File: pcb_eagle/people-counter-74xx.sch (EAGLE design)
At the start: 13 parts, among them IC1 74LS90N, IC2 74LS47N

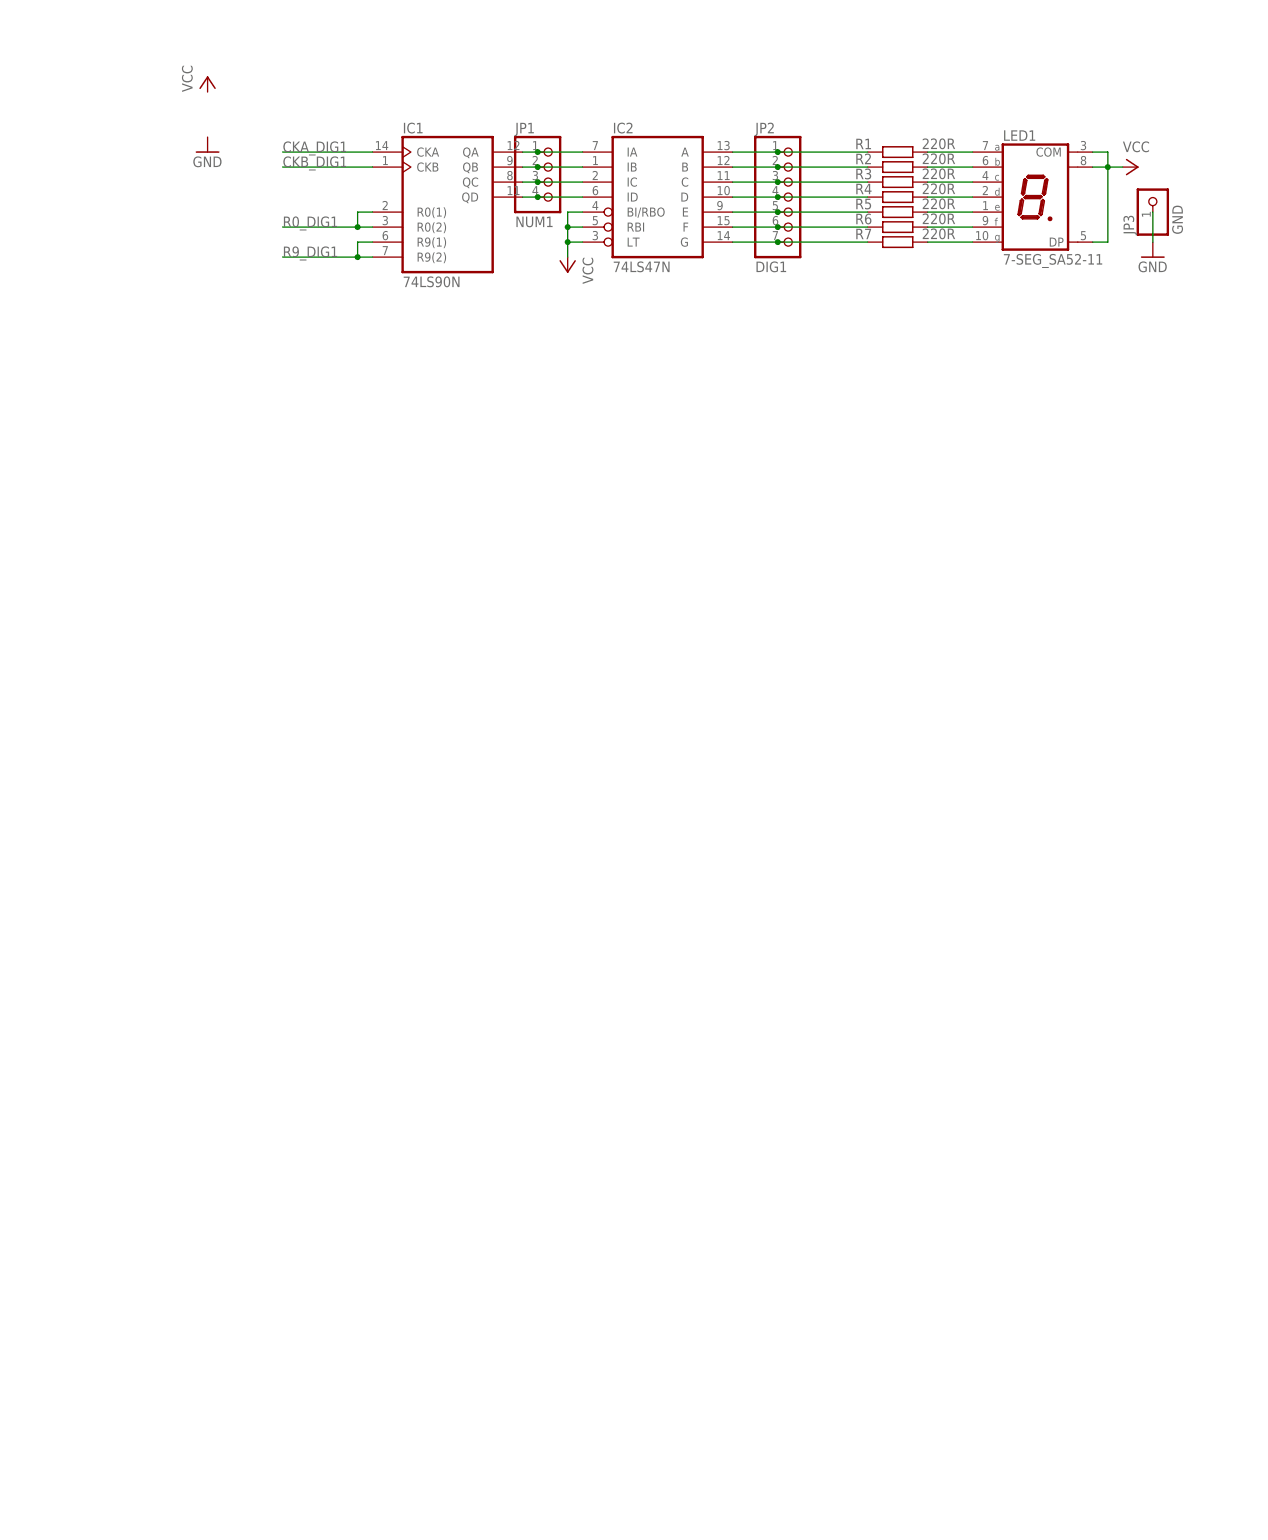
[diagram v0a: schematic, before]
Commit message: PCB_EAGLE: finish layout of 4 design module (LED segment counter}
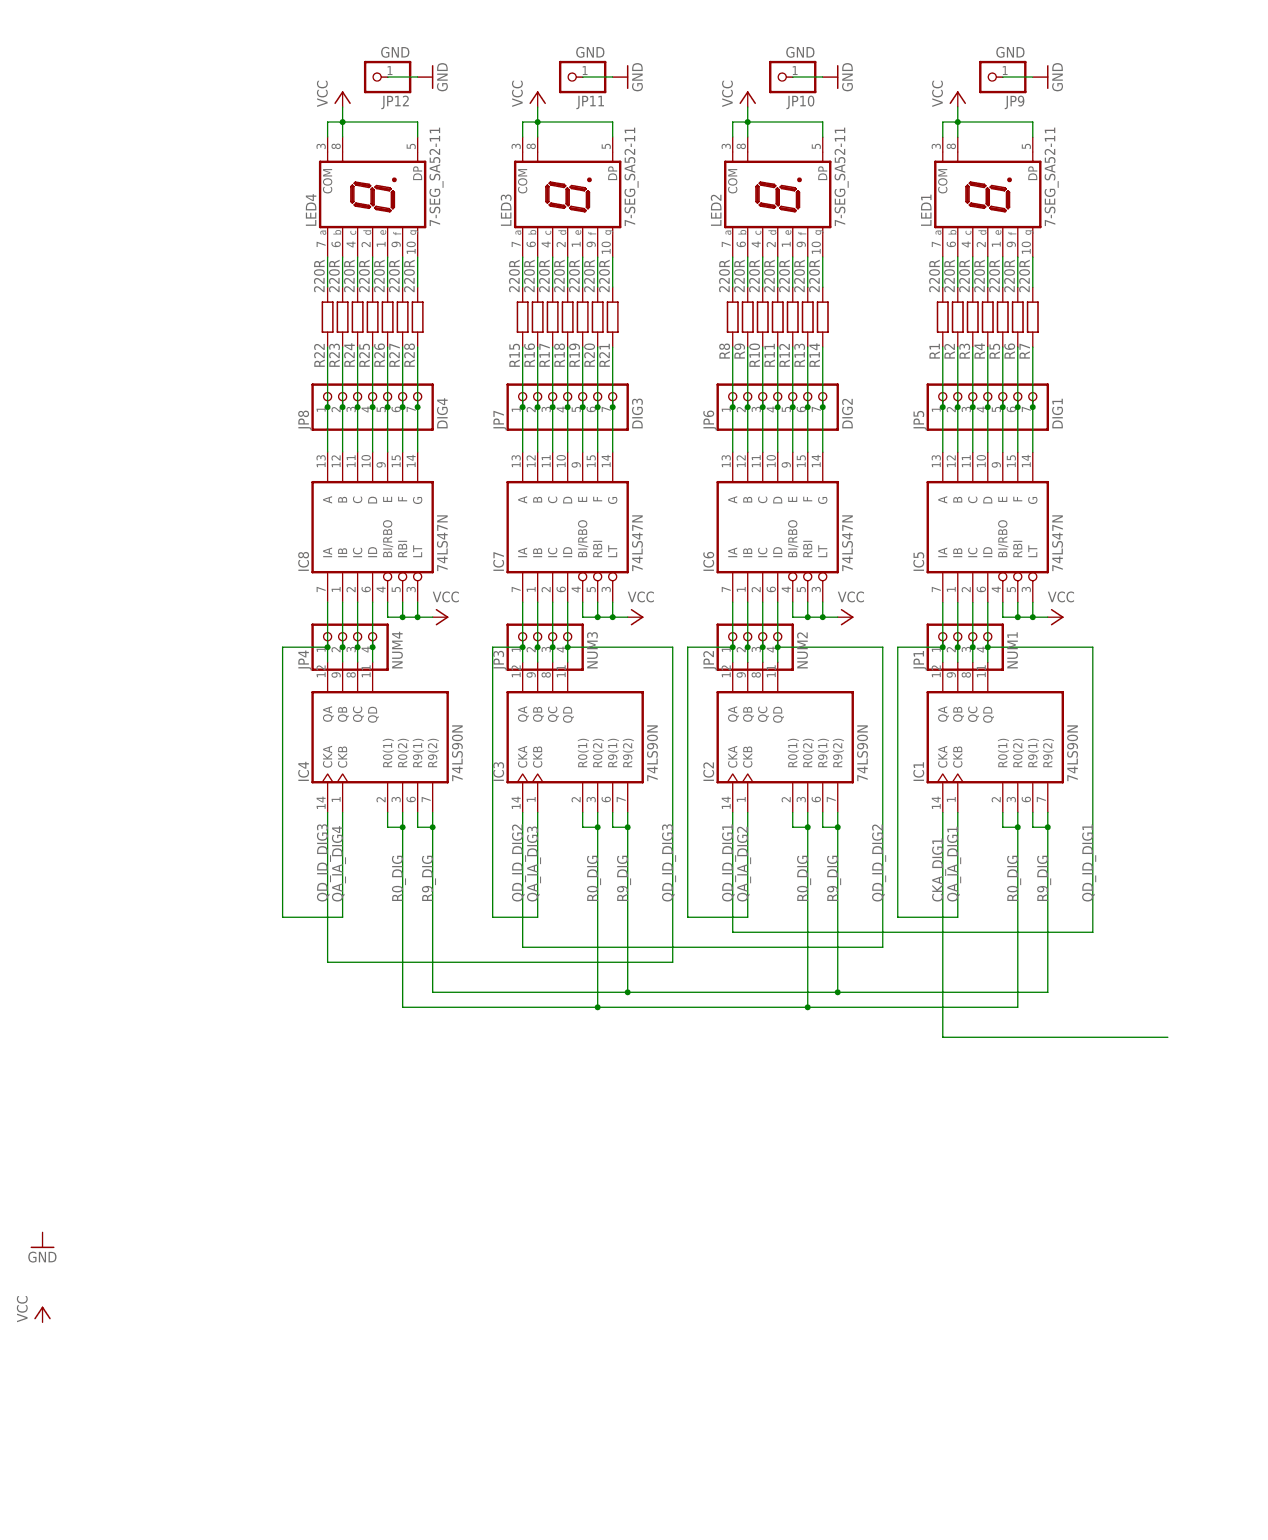
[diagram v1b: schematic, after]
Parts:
- added IC3, IC4: 74LS90N, 74xx-eu:74LS90N
- added IC5, IC6, IC7, IC8: 74LS47N, 74xx-eu:74LS47N
- added JP10, JP11, JP12, JP9: GND, pinhead:PINHD-1X1
- added JP4: NUM4, pinhead:PINHD-1X4
- added JP5: DIG1, pinhead:PINHD-1X7
- added JP6: DIG2, pinhead:PINHD-1X7
- added JP7: DIG3, pinhead:PINHD-1X7
- added JP8: DIG4, pinhead:PINHD-1X7
- added LED2, LED3, LED4: 7-SEG_SA52-11, display-kingbright:7-SEG_SA52-11
- added R10, R11, R12, R13, R14, R15, R16, R17, R18, R19, R20, R21, R22, R23, R24, R25, R26, R27, R28, R8, R9: 220R, rcl:R-EU_R0603
- IC2: value 74LS47N -> 74LS90N; device 74xx-eu:74LS47N -> 74xx-eu:74LS90N
- JP2: value DIG1 -> NUM2; device pinhead:PINHD-1X7 -> pinhead:PINHD-1X4
- JP3: value GND -> NUM3; device pinhead:PINHD-1X1 -> pinhead:PINHD-1X4
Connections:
- removed net CKB_DIG1: IC1A.CKB
- removed net R0_DIG1: IC1A.R0(1), IC1A.R0(2)
- removed net R9_DIG1: IC1A.R9(1), IC1A.R9(2)
- new net A_DIG2: IC6G$1.A, JP6.1, R8.1
- new net A_DIG3: IC7G$1.A, JP7.1, R15.1
- new net A_DIG4: IC8G$1.A, JP8.1, R22.1
- new net A_DIG_2: LED2.A, R8.2
- new net A_DIG_3: LED3.A, R15.2
- new net A_DIG_4: LED4.A, R22.2
- new net B_DIG2: IC6G$1.B, JP6.2, R9.1
- new net B_DIG3: IC7G$1.B, JP7.2, R16.1
- new net B_DIG4: IC8G$1.B, JP8.2, R23.1
- new net B_DIG_2: LED2.B, R9.2
- new net B_DIG_3: LED3.B, R16.2
- new net B_DIG_4: LED4.B, R23.2
- new net C_DIG2: IC6G$1.C, JP6.3, R10.1
- new net C_DIG3: IC7G$1.C, JP7.3, R17.1
- new net C_DIG4: IC8G$1.C, JP8.3, R24.1
- new net C_DIG_2: LED2.C, R10.2
- new net C_DIG_3: LED3.C, R17.2
- new net C_DIG_4: LED4.C, R24.2
- new net D_DIG2: IC6G$1.D, JP6.4, R11.1
- new net D_DIG3: IC7G$1.D, JP7.4, R18.1
- new net D_DIG4: IC8G$1.D, JP8.4, R25.1
- new net D_DIG_2: LED2.D, R11.2
- new net D_DIG_3: LED3.D, R18.2
- new net D_DIG_4: LED4.D, R25.2
- new net E_DIG2: IC6G$1.E, JP6.5, R12.1
- new net E_DIG3: IC7G$1.E, JP7.5, R19.1
- new net E_DIG4: IC8G$1.E, JP8.5, R26.1
- new net E_DIG_2: LED2.E, R12.2
- new net E_DIG_3: LED3.E, R19.2
- new net E_DIG_4: LED4.E, R26.2
- new net F_DIG2: IC6G$1.F, JP6.6, R13.1
- new net F_DIG3: IC7G$1.F, JP7.6, R20.1
- new net F_DIG4: IC8G$1.F, JP8.6, R27.1
- new net F_DIG_2: LED2.F, R13.2
- new net F_DIG_3: LED3.F, R20.2
- new net F_DIG_4: LED4.F, R27.2
- new net G_DIG2: IC6G$1.G, JP6.7, R14.1
- new net G_DIG3: IC7G$1.G, JP7.7, R21.1
- new net G_DIG4: IC8G$1.G, JP8.7, R28.1
- new net G_DIG_2: LED2.G, R14.2
- new net G_DIG_3: LED3.G, R21.2
- new net G_DIG_4: LED4.G, R28.2
- new net QA_IA_DIG2: IC2A.CKB, IC2A.QA, IC6G$1.IA, JP2.1
- new net QA_IA_DIG3: IC3A.CKB, IC3A.QA, IC7G$1.IA, JP3.1
- new net QA_IA_DIG4: IC4A.CKB, IC4A.QA, IC8G$1.IA, JP4.1
- new net QB_IB_DIG2: IC2A.QB, IC6G$1.IB, JP2.2
- new net QB_IB_DIG3: IC3A.QB, IC7G$1.IB, JP3.2
- new net QB_IB_DIG4: IC4A.QB, IC8G$1.IB, JP4.2
- new net QC_IC_DIG2: IC2A.QC, IC6G$1.IC, JP2.3
- new net QC_IC_DIG3: IC3A.QC, IC7G$1.IC, JP3.3
- new net QC_IC_DIG4: IC4A.QC, IC8G$1.IC, JP4.3
- new net QD_ID_DIG2: IC2A.QD, IC3A.CKA, IC6G$1.ID, JP2.4
- new net QD_ID_DIG3: IC3A.QD, IC4A.CKA, IC7G$1.ID, JP3.4
- new net QD_ID_DIG4: IC4A.QD, IC8G$1.ID, JP4.4
- new net R0_DIG: IC1A.R0(1), IC1A.R0(2), IC2A.R0(1), IC2A.R0(2), IC3A.R0(1), IC3A.R0(2), IC4A.R0(1), IC4A.R0(2)
- new net R9_DIG: IC1A.R9(1), IC1A.R9(2), IC2A.R9(1), IC2A.R9(2), IC3A.R9(1), IC3A.R9(2), IC4A.R9(1), IC4A.R9(2)
- net A_DIG1: now also IC5G$1.A, JP5.1; no longer IC2G$1.A, JP2.1
- net B_DIG1: now also IC5G$1.B, JP5.2; no longer IC2G$1.B, JP2.2
- net C_DIG1: now also IC5G$1.C, JP5.3; no longer IC2G$1.C, JP2.3
- net D_DIG1: now also IC5G$1.D, JP5.4; no longer IC2G$1.D, JP2.4
- net E_DIG1: now also IC5G$1.E, JP5.5; no longer IC2G$1.E, JP2.5
- net F_DIG1: now also IC5G$1.F, JP5.6; no longer IC2G$1.F, JP2.6
- net GND: now also JP10.1, JP11.1, JP12.1, JP9.1; no longer JP3.1
- net G_DIG1: now also IC5G$1.G, JP5.7; no longer IC2G$1.G, JP2.7
- net QA_IA_DIG1: now also IC1A.CKB, IC5G$1.IA; no longer IC2G$1.IA
- net QB_IB_DIG1: now also IC5G$1.IB; no longer IC2G$1.IB
- net QC_IC_DIG1: now also IC5G$1.IC; no longer IC2G$1.IC
- net QD_ID_DIG1: now also IC2A.CKA, IC5G$1.ID; no longer IC2G$1.ID
- net VCC: now also IC5G$1.BI/RBO, IC5G$1.LT, IC5G$1.RBI, IC6G$1.BI/RBO, IC6G$1.LT, IC6G$1.RBI, IC7G$1.BI/RBO, IC7G$1.LT, IC7G$1.RBI, IC8G$1.BI/RBO, IC8G$1.LT, IC8G$1.RBI, LED2.COM@1, LED2.COM@2, LED2.DP, LED3.COM@1, LED3.COM@2, LED3.DP, LED4.COM@1, LED4.COM@2, LED4.DP; no longer IC2G$1.BI/RBO, IC2G$1.LT, IC2G$1.RBI
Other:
- moved on the sheet: IC1, JP1, LED1, R1, R2, R3, R4, R5, R6, R7

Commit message: PCB_EAGLE: add frequency square wave generator based on the NE555 and some connectors to schema
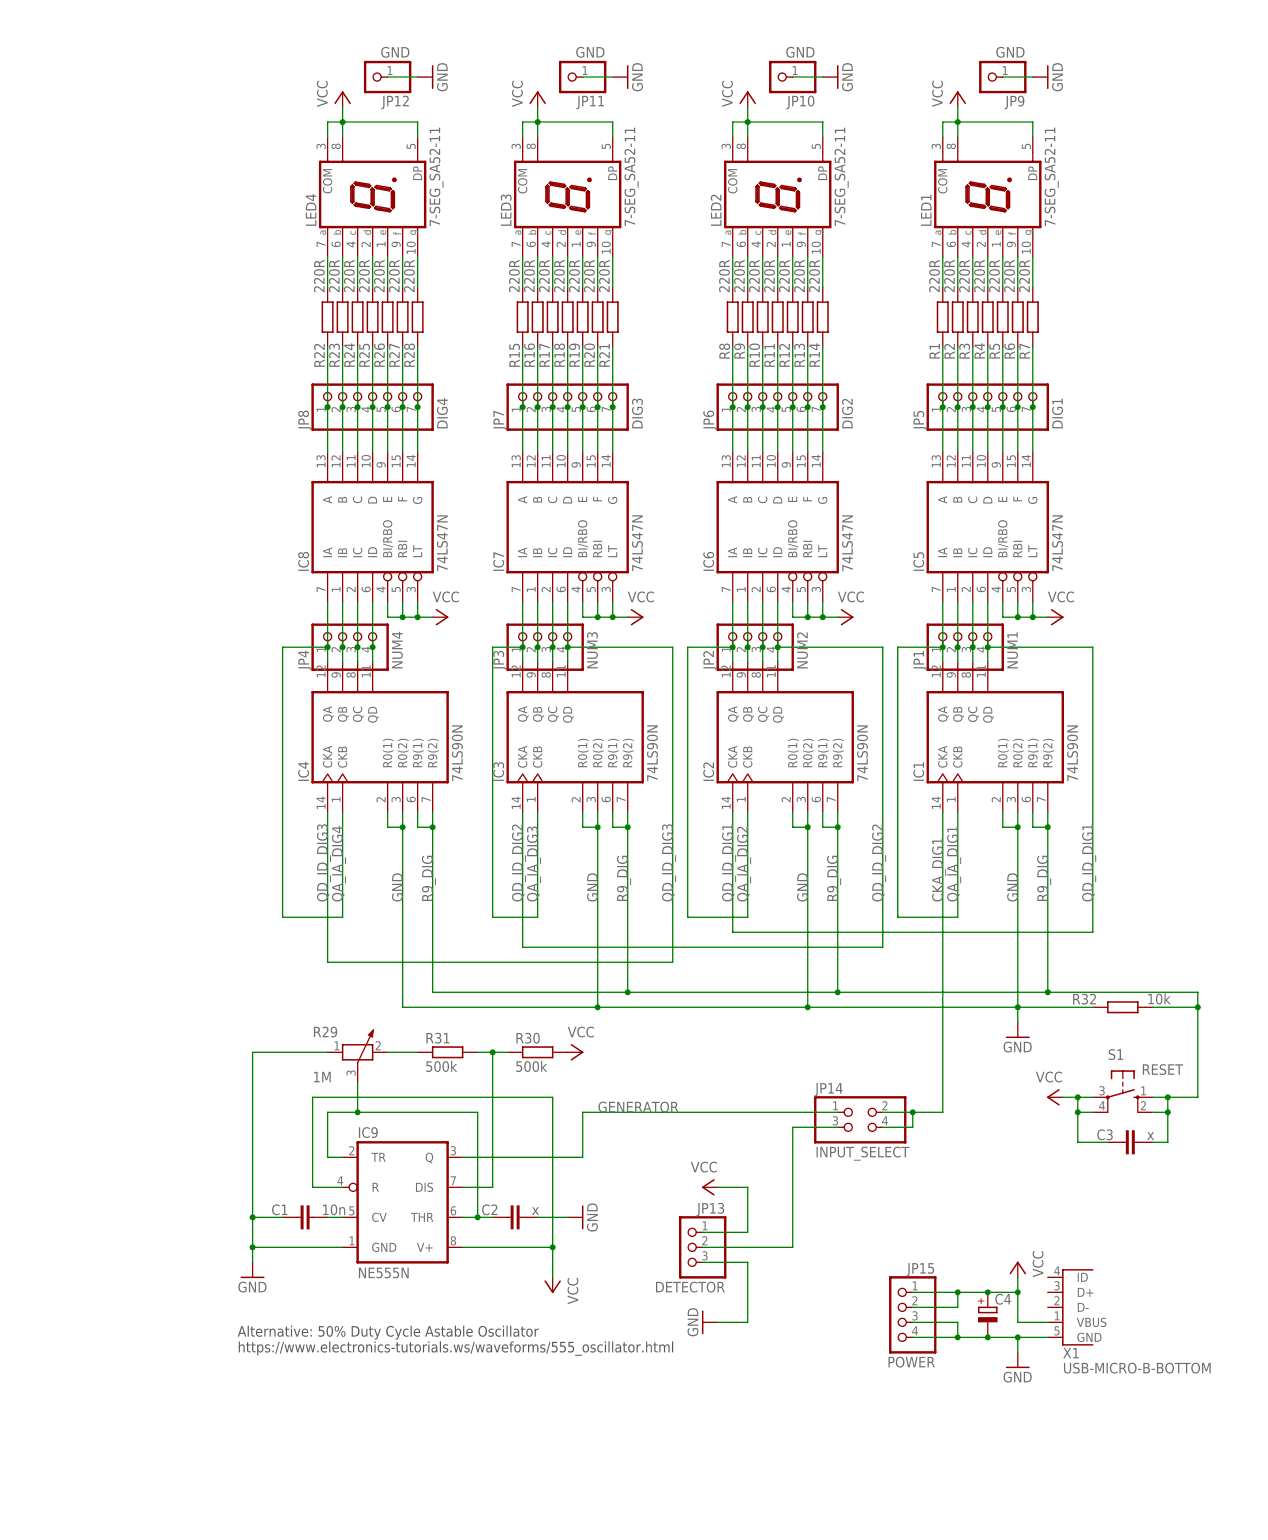
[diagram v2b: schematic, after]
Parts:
- added C1: 10n, rcl:C-EUC0603
- added C2, C3: x, rcl:C-EUC0603
- added C4: (no value), rcl:CPOL-EUE5-10.5
- added IC9: NE555N, linear:NE555N
- added JP13: DETECTOR, pinhead:PINHD-1X3/90
- added JP14: INPUT_SELECT, pinhead:PINHD-2X2
- added JP15: POWER, pinhead:PINHD-1X4/90
- added R29: 1M, rcl:POTENTIOMETER_PT-10
- added R30, R31: 500k, rcl:R-EU_R0603
- added R32: 10k, rcl:R-EU_R0603
- added S1: RESET, switch-omron:10-XX
- added X1: USB-MICRO-B-BOTTOM, usb:USB-MICRO-B-BOTTOM
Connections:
- removed net R0_DIG: IC1A.R0(1), IC1A.R0(2), IC2A.R0(1), IC2A.R0(2), IC3A.R0(1), IC3A.R0(2), IC4A.R0(1), IC4A.R0(2)
- new net GENERATOR: IC9.Q, JP14.1
- new net N$2: R29.2, R31.1
- new net N$3: C2.1, IC9.THR, IC9.TR, R29.3
- new net N$4: C1.2, IC9.CV
- new net N$5: JP13.2, JP14.3
- new net N$6: IC9.DIS, R30.1, R31.2
- net CKA_DIG1: now also JP14.2, JP14.4
- net GND: now also C1.1, C2.2, C4.-, IC1A.R0(1), IC1A.R0(2), IC2A.R0(1), IC2A.R0(2), IC3A.R0(1), IC3A.R0(2), IC4A.R0(1), IC4A.R0(2), IC9.GND, JP13.3, JP15.3, JP15.4, R29.1, R32.1, X1.GND
- net R9_DIG: now also C3.2, R32.2, S1.S, S1.S1
- net VCC: now also C3.1, C4.+, IC9.R, IC9.V+, JP13.1, JP15.1, JP15.2, R30.2, S1.P, S1.P1, X1.VBUS
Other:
- note added: "Alternative: 50% Duty Cycle Astable Oscillator https://www.electronics-tutorials.ws/waveforms/555_oscillator.html"
